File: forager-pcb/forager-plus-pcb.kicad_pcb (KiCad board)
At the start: 2 copper layers, 114.6 x 96.3 mm, 27 parts, among them J2 Conn_01x02_Pin, U1 XIAO nRF52840 Plus

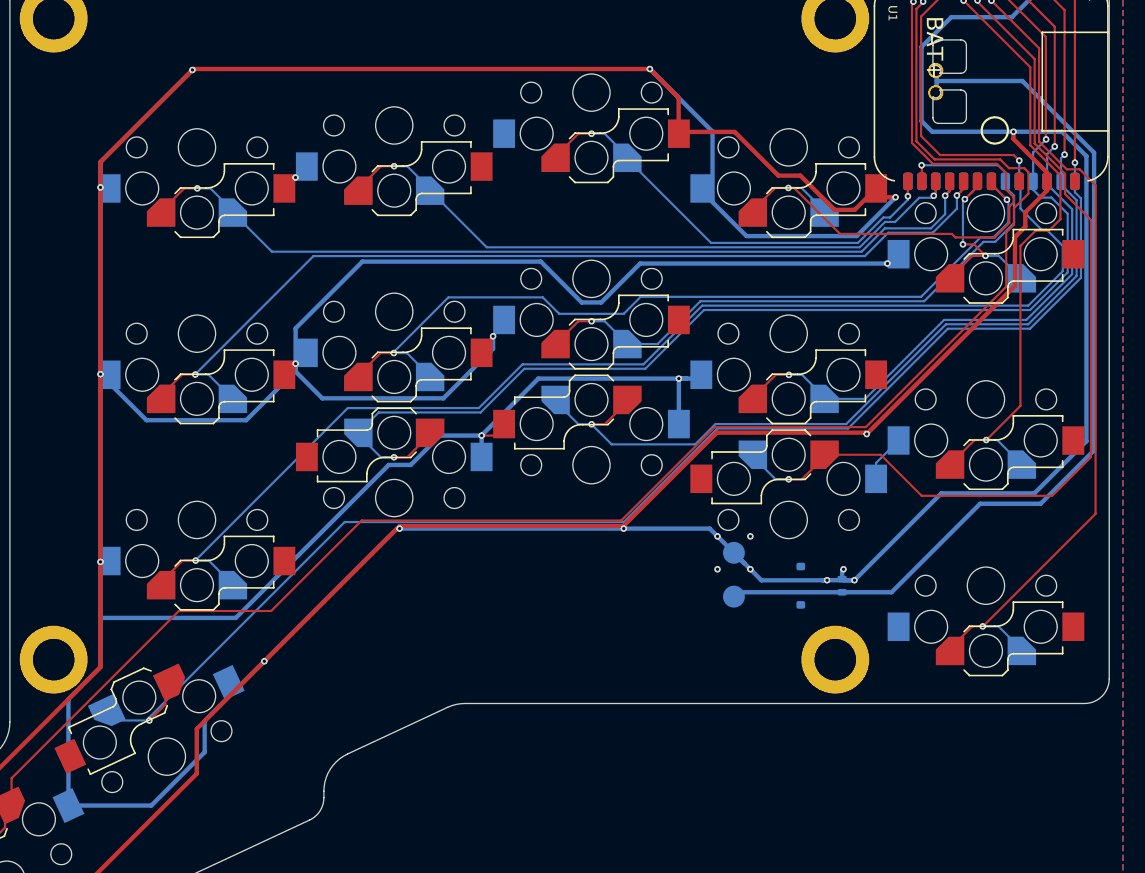
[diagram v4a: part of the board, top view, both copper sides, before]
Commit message: Solved potential ground plane issue with explicit tracks
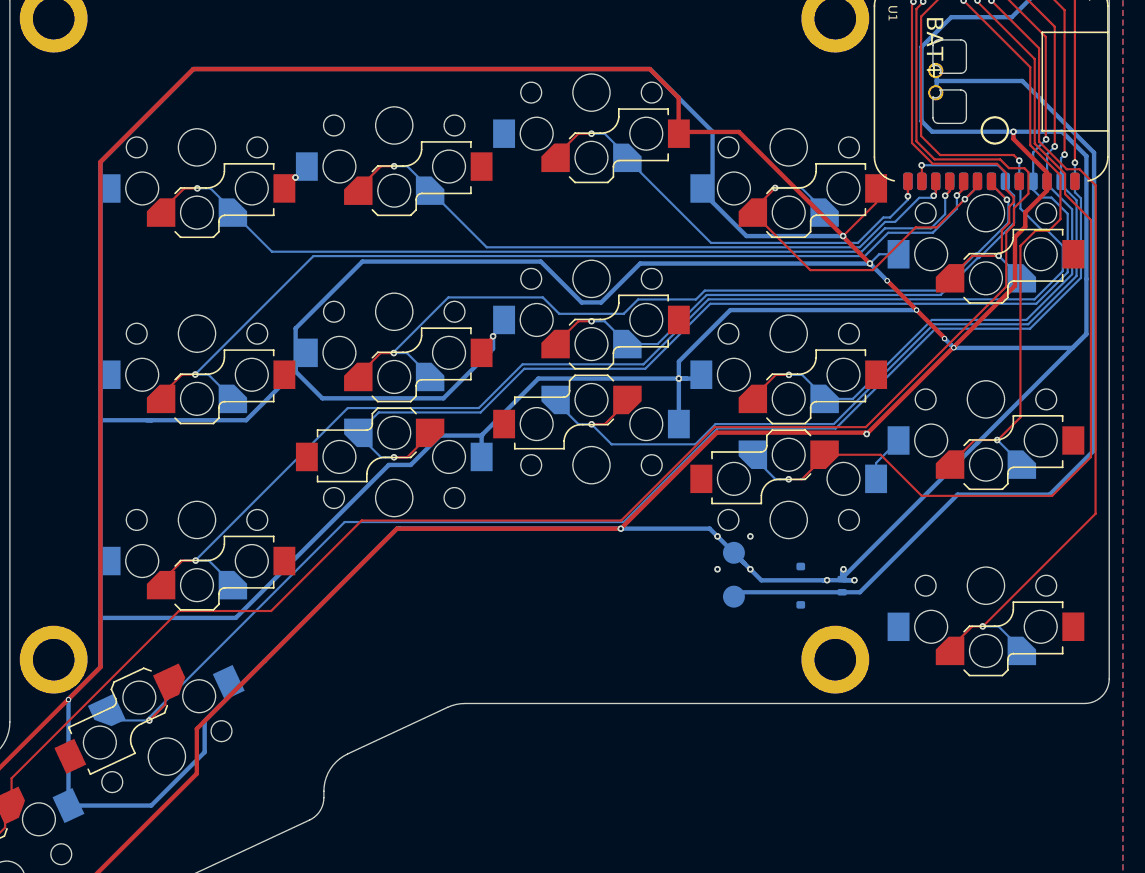
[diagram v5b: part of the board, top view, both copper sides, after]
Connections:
- U1 pad 21: RT4 -> RT3
- U1 pad 7: RT3 -> RT4
- U1 pad 14: RT3 -> RT4
- U1 pad 18: RT4 -> RT3
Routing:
- net GND: track 777.8 -> 856.4 mm, vias 24 -> 20
- net RT3: track 62.5 -> 35.7 mm
- net RT4: track 18.2 -> 43.4 mm, vias 3 -> 2

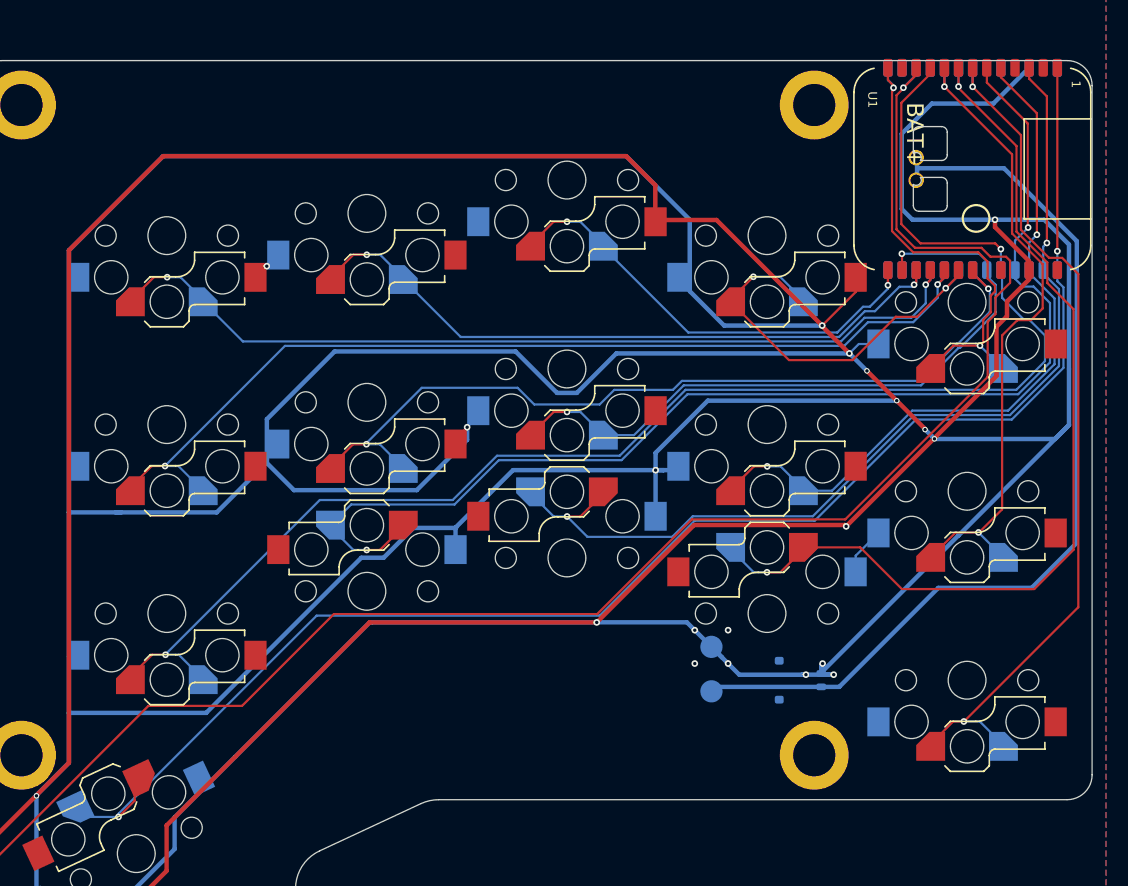
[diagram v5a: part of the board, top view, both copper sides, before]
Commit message: Restore cutout and one set of 4 labels under USB
These are CLK, DIO, GND, RST - can't connect GND due to mirroring
with RST.
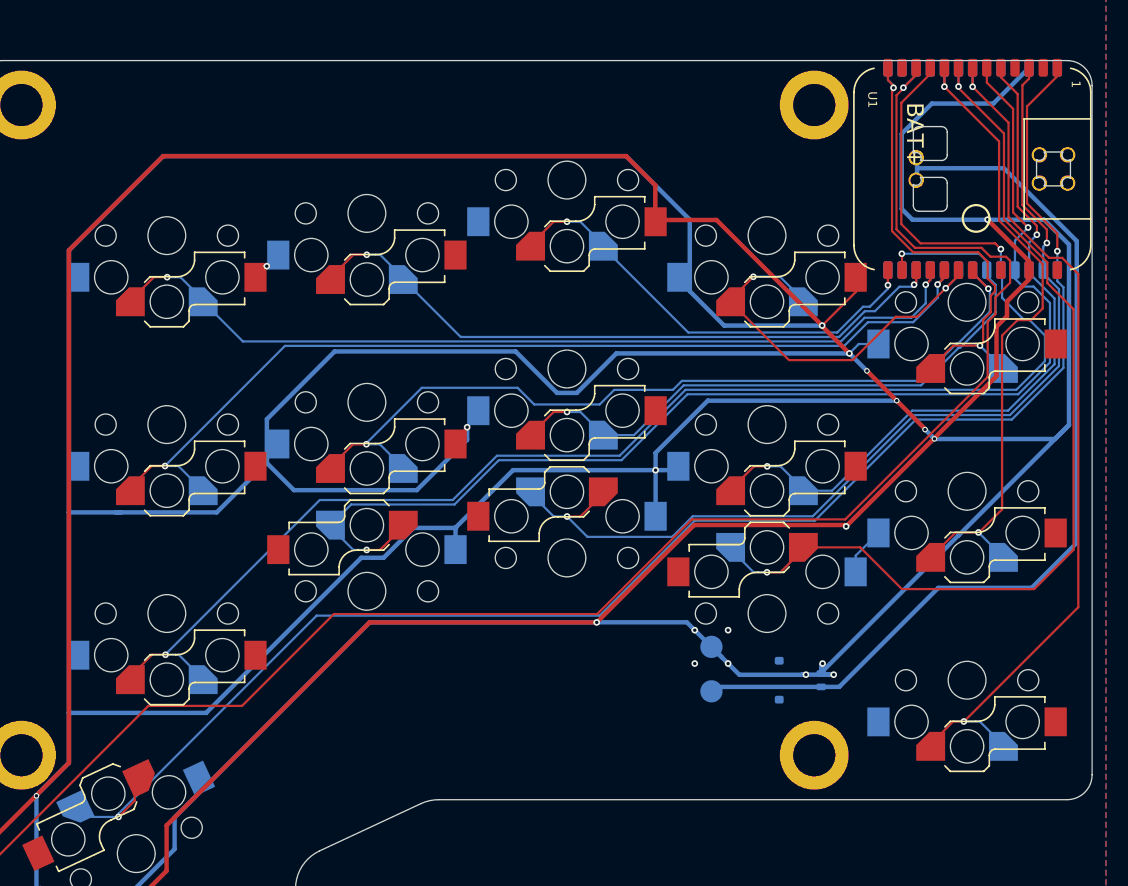
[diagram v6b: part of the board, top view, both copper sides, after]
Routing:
- net RH1: track 135.8 -> 138.1 mm
- net GND: track 856.4 -> 855.9 mm

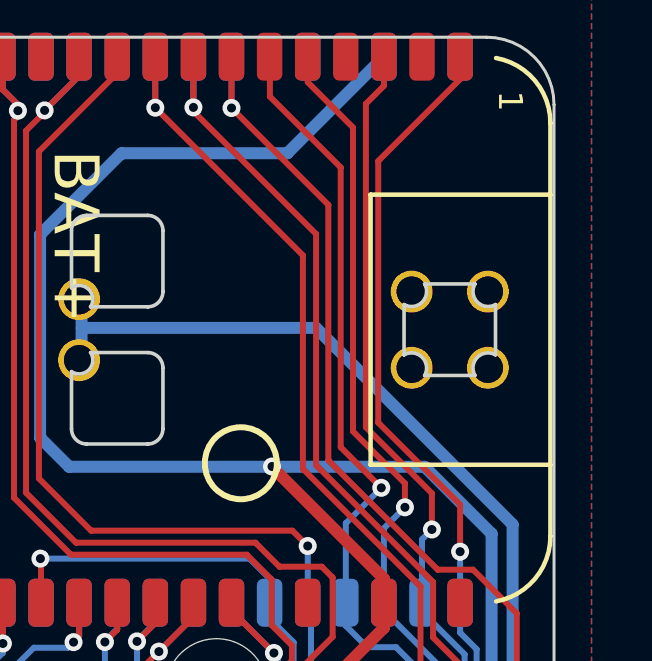
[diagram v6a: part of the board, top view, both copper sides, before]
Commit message: Restore second set of 4 labels under USB
These are CLK, DIO, GND, RST - can't connect GND due to mirroring
with RST.
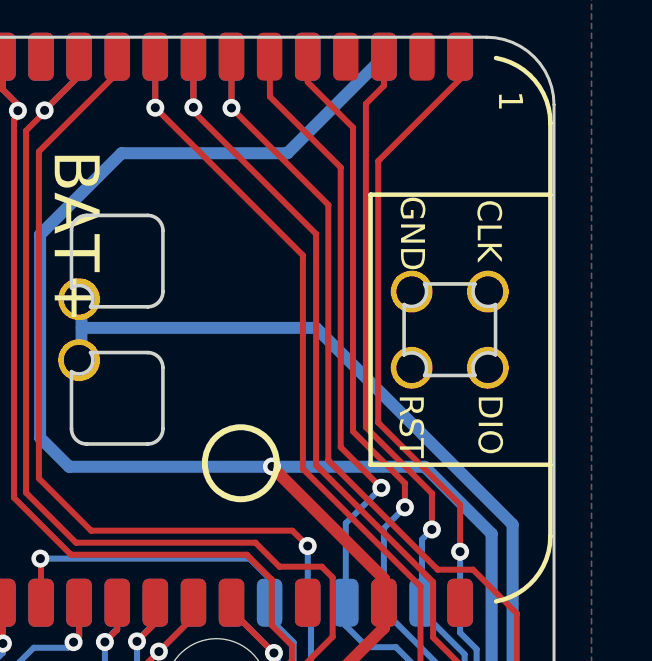
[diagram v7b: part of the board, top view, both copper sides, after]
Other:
- board text added: "CLK"
- board text added: "DIO"
- board text added: "GND"
- board text added: "RST"
